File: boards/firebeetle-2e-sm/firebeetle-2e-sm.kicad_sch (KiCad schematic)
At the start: 13 parts, among them J1 Power In, J2 Wiegand, J3 Feedback, J4 Button, J5 Relay, U1 DFR0654, U2 MP1584EN Module

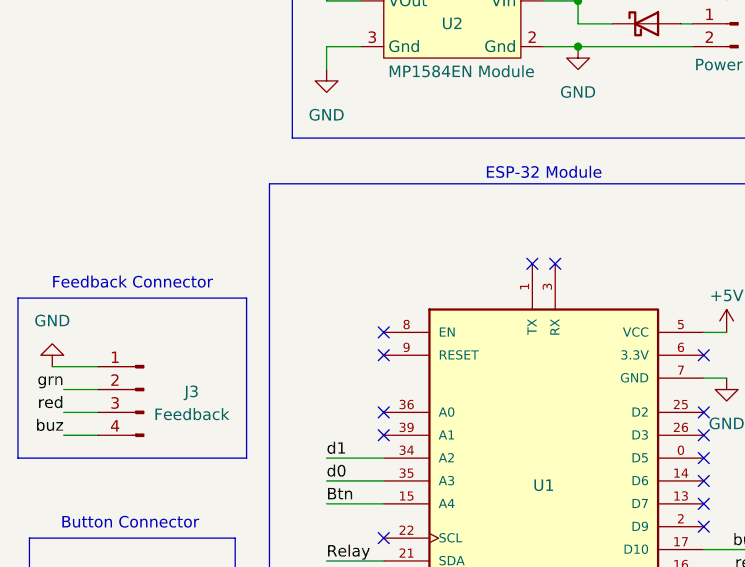
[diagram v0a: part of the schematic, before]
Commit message: Added 10uF capacitor between reset and ground to handle slow power supply
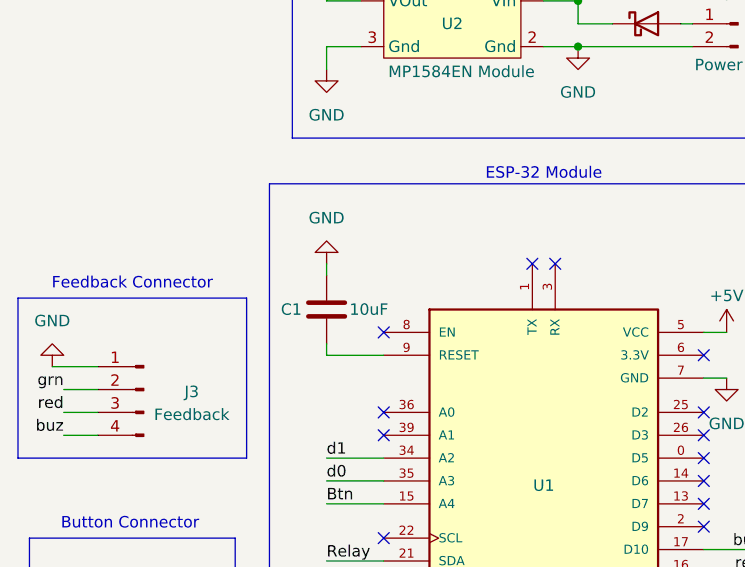
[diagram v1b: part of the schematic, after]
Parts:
- added C1: 10uF, Capacitor_SMD:C_0805_2012Metric_Pad1.18x1.45mm_HandSolder, symbol Device:C
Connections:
- net GND: now also C1.1
- net at U1.9 (RESET): now also C1.2
- no-connect marks 18 -> 17
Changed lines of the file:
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@@
-	)
-	(no_connect
-		(at 60.96 66.04)
 	)
 	(no_connect
@@
 	(wire
 		(pts
+			(xy 54.61 57.15) (xy 54.61 55.88)
+		)
+		(stroke
+			(width 0)
+			(type default)
+		)
+	)
+	(wire
+		(pts
 			(xy 134.62 88.9) (xy 134.62 91.44)
 		)
@@
 	(wire
 		(pts
+			(xy 54.61 64.77) (xy 54.61 66.04)
+		)
+		(stroke
+			(width 0)
+			(type default)
+		)
+	)
+	(wire
+		(pts
 			(xy 132.08 57.15) (xy 134.62 57.15)
 		)
@@
 		(pts
 			(xy 128.27 91.44) (xy 134.62 91.44)
+		)
+		(stroke
+			(width 0)
+			(type default)
+		)
+	)
+	(wire
+		(pts
+			(xy 54.61 66.04) (xy 60.96 66.04)
 		)
 		(stroke
@@
 				(path "/0df1a8ca-d4c3-4202-9e1e-dfe87dcb7bf9"
 					(reference "J3")
+					(unit 1)
+				)
+			)
+		)
+	)
+	(symbol
+		(lib_id "Device:C")
+		(at 54.61 60.96 0)
+		(unit 1)
+		(exclude_from_sim no)
+		(in_bom yes)
+		(on_board yes)
+		(dnp no)
+		(property "Reference" "C1"
+			(at 49.53 60.96 0)
+			(effects
+				(font
+					(size 1.27 1.27)
+				)
+				(justify left)
+			)
+		)
+		(property "Value" "10uF"
+			(at 57.15 60.96 0)
+			(effects
+				(font
+					(size 1.27 1.27)
+				)
+				(justify left)
+			)
+		)
+		(property "Footprint" "Capacitor_SMD:C_0805_2012Metric_Pad1.18x1.45mm_HandSolder"
+			(at 55.5752 64.77 0)
+			(effects
+				(font
+					(size 1.27 1.27)
+				)
+				(hide yes)
+			)
+		)
+		(property "Datasheet" "~"
+			(at 54.61 60.96 0)
+			(effects
+				(font
+					(size 1.27 1.27)
+				)
+				(hide yes)
+			)
+		)
+		(property "Description" "Unpolarized capacitor"
+			(at 54.61 60.96 0)
+			(effects
+				(font
+					(size 1.27 1.27)
+				)
+				(hide yes)
+			)
+		)
+		(pin "2"
+		)
+		(pin "1"
+		)
+		(instances
+			(project ""
+				(path "/0df1a8ca-d4c3-4202-9e1e-dfe87dcb7bf9"
+					(reference "C1")
 					(unit 1)
 				)
@@
 					(unit 1)
 				)
+			)
+		)
+	)
+	(symbol
+		(lib_id "power:GND")
+		(at 54.61 55.88 180)
+		(unit 1)
+		(exclude_from_sim no)
+		(in_bom yes)
+		(on_board yes)
+		(dnp no)
+		(property "Reference" "#PWR014"
+			(at 54.61 49.53 0)
+			(effects
+				(font
+					(size 1.27 1.27)
+				)
+				(hide yes)
+			)
+		)
+		(property "Value" "GND"
+			(at 54.61 50.8 0)
+			(effects
+				(font
+					(size 1.27 1.27)
+				)
+			)
+		)
+		(property "Footprint" ""
+			(at 54.61 55.88 0)
+			(effects
+				(font
+					(size 1.27 1.27)
+				)
+				(hide yes)
+			)
+		)
+		(property "Datasheet" ""
+			(at 54.61 55.88 0)
+			(effects
+				(font
+					(size 1.27 1.27)
+				)
+				(hide yes)
+			)
+		)
+		(property "Description" "Power symbol creates a global label with name \"GND\" , ground"
+			(at 54.61 55.88 0)
+			(effects
+				(font
+					(size 1.27 1.27)
+				)
+				(hide yes)
+			)
+		)
+		(pin "1"
+		)
+		(instances
+			(project "firebeetle-2e-sm"
+				(path "/0df1a8ca-d4c3-4202-9e1e-dfe87dcb7bf9"
+					(reference "#PWR014")
+					(unit 1)
+				)

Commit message: Revert EN capacitor, update firebeetle th, updated documentation to remove MP2307EN SS capacitor
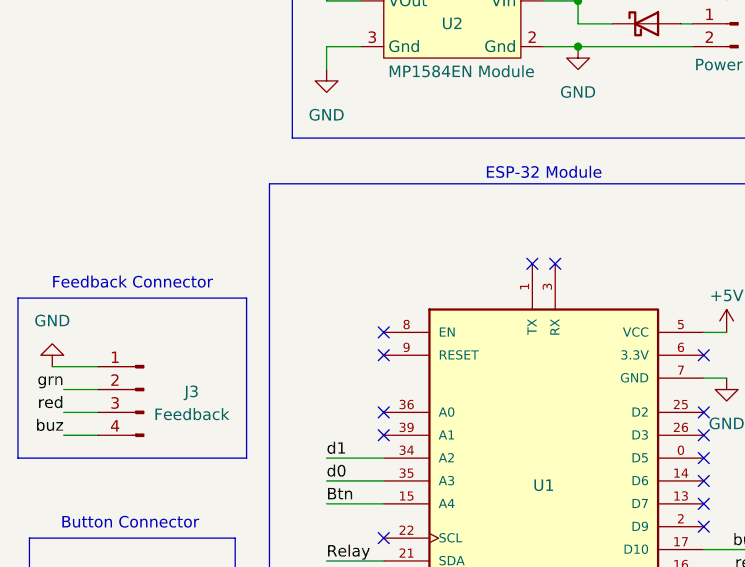
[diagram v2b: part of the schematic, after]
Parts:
- removed C1: 10uF, Capacitor_SMD:C_0805_2012Metric_Pad1.18x1.45mm_HandSolder, symbol Device:C
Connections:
- no-connect marks 17 -> 18
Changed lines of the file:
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@@
+	)
+	(no_connect
+		(at 60.96 66.04)
 	)
 	(no_connect
@@
 	(wire
 		(pts
-			(xy 54.61 57.15) (xy 54.61 55.88)
-		)
-		(stroke
-			(width 0)
-			(type default)
-		)
-	)
-	(wire
-		(pts
 			(xy 134.62 88.9) (xy 134.62 91.44)
 		)
@@
 	(wire
 		(pts
-			(xy 54.61 64.77) (xy 54.61 66.04)
-		)
-		(stroke
-			(width 0)
-			(type default)
-		)
-	)
-	(wire
-		(pts
 			(xy 132.08 57.15) (xy 134.62 57.15)
 		)
@@
 		(pts
 			(xy 128.27 91.44) (xy 134.62 91.44)
-		)
-		(stroke
-			(width 0)
-			(type default)
-		)
-	)
-	(wire
-		(pts
-			(xy 54.61 66.04) (xy 60.96 66.04)
 		)
 		(stroke
@@
 				(path "/0df1a8ca-d4c3-4202-9e1e-dfe87dcb7bf9"
 					(reference "J3")
-					(unit 1)
-				)
-			)
-		)
-	)
-	(symbol
-		(lib_id "Device:C")
-		(at 54.61 60.96 0)
-		(unit 1)
-		(exclude_from_sim no)
-		(in_bom yes)
-		(on_board yes)
-		(dnp no)
-		(property "Reference" "C1"
-			(at 49.53 60.96 0)
-			(effects
-				(font
-					(size 1.27 1.27)
-				)
-				(justify left)
-			)
-		)
-		(property "Value" "10uF"
-			(at 57.15 60.96 0)
-			(effects
-				(font
-					(size 1.27 1.27)
-				)
-				(justify left)
-			)
-		)
-		(property "Footprint" "Capacitor_SMD:C_0805_2012Metric_Pad1.18x1.45mm_HandSolder"
-			(at 55.5752 64.77 0)
-			(effects
-				(font
-					(size 1.27 1.27)
-				)
-				(hide yes)
-			)
-		)
-		(property "Datasheet" "~"
-			(at 54.61 60.96 0)
-			(effects
-				(font
-					(size 1.27 1.27)
-				)
-				(hide yes)
-			)
-		)
-		(property "Description" "Unpolarized capacitor"
-			(at 54.61 60.96 0)
-			(effects
-				(font
-					(size 1.27 1.27)
-				)
-				(hide yes)
-			)
-		)
-		(pin "2"
-		)
-		(pin "1"
-		)
-		(instances
-			(project ""
-				(path "/0df1a8ca-d4c3-4202-9e1e-dfe87dcb7bf9"
-					(reference "C1")
 					(unit 1)
 				)
@@
 					(unit 1)
 				)
-			)
-		)
-	)
-	(symbol
-		(lib_id "power:GND")
-		(at 54.61 55.88 180)
-		(unit 1)
-		(exclude_from_sim no)
-		(in_bom yes)
-		(on_board yes)
-		(dnp no)
-		(property "Reference" "#PWR014"
-			(at 54.61 49.53 0)
-			(effects
-				(font
-					(size 1.27 1.27)
-				)
-				(hide yes)
-			)
-		)
-		(property "Value" "GND"
-			(at 54.61 50.8 0)
-			(effects
-				(font
-					(size 1.27 1.27)
-				)
-			)
-		)
-		(property "Footprint" ""
-			(at 54.61 55.88 0)
-			(effects
-				(font
-					(size 1.27 1.27)
-				)
-				(hide yes)
-			)
-		)
-		(property "Datasheet" ""
-			(at 54.61 55.88 0)
-			(effects
-				(font
-					(size 1.27 1.27)
-				)
-				(hide yes)
-			)
-		)
-		(property "Description" "Power symbol creates a global label with name \"GND\" , ground"
-			(at 54.61 55.88 0)
-			(effects
-				(font
-					(size 1.27 1.27)
-				)
-				(hide yes)
-			)
-		)
-		(pin "1"
-		)
-		(instances
-			(project "firebeetle-2e-sm"
-				(path "/0df1a8ca-d4c3-4202-9e1e-dfe87dcb7bf9"
-					(reference "#PWR014")
-					(unit 1)
-				)
